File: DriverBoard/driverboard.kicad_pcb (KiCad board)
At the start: 2 copper layers, 95 x 95 mm, 93 parts, among them J1 USB_C_Receptacle_USB2.0_14P, J2 Conn_01x02_Pin, J3 Conn_02x05_Counter_Clockwise, J4 Conn_02x05_Counter_Clockwise, J5 Conn_02x05_Counter_Clockwise, J6 Conn_01x08_Pin, J7 Conn_01x08_Pin, J8 Conn_01x08_Pin, J9 Conn_01x08_Pin, Q1 DMG2305UX, Q2 DMG2305UX, Q3 SL3402, Q4 SL3402, Q5 SL3402, Q6 SL3402, U1 LM556, U10 74HC595, U11 TBD62783A, U2 MC34063AD, U3 TLV274, U4 74HC595, U5 TBD62783A, U6 74HC595, U7 TBD62783A, U8 74HC595, U9 TBD62783A

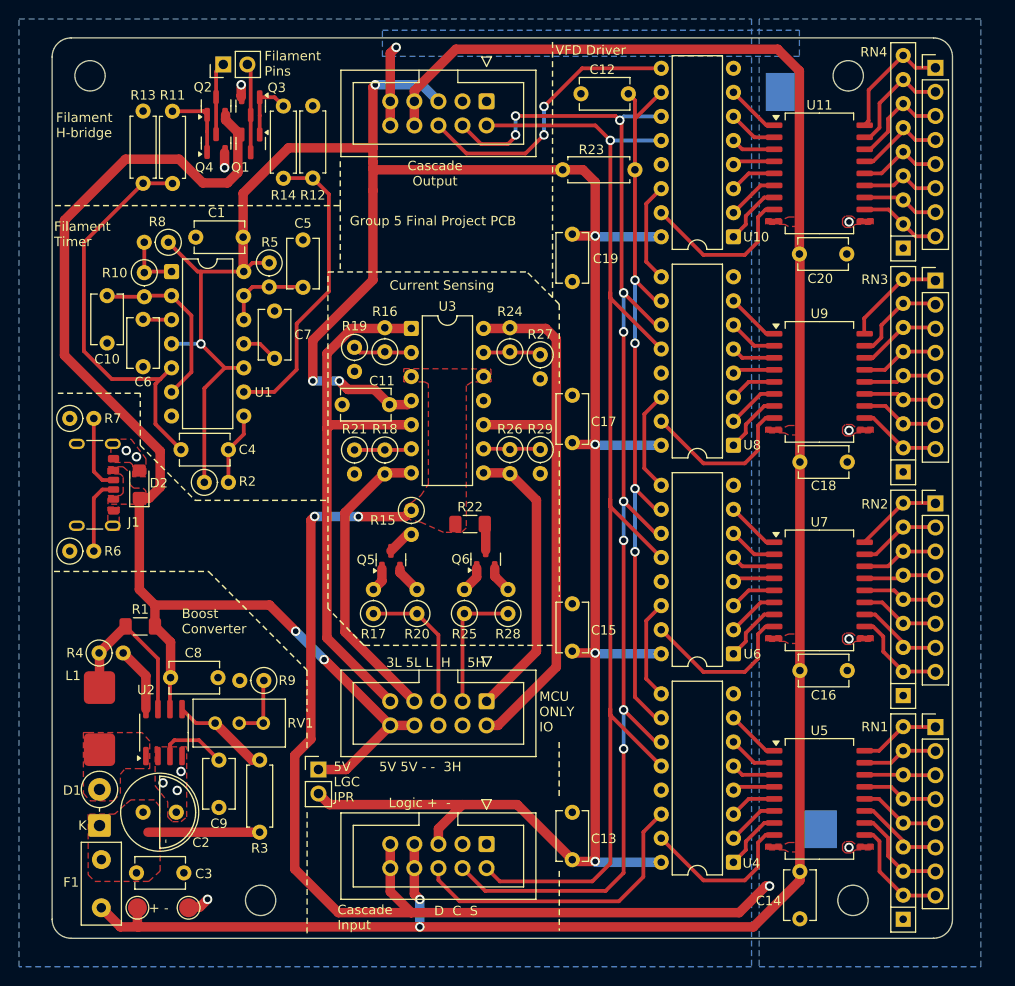
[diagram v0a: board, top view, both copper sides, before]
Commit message: Minor PCB rev
Moved shift register bypass caps around a bit. Also changed a price on
the BOM, that's the final change before the digikey parts order is in.
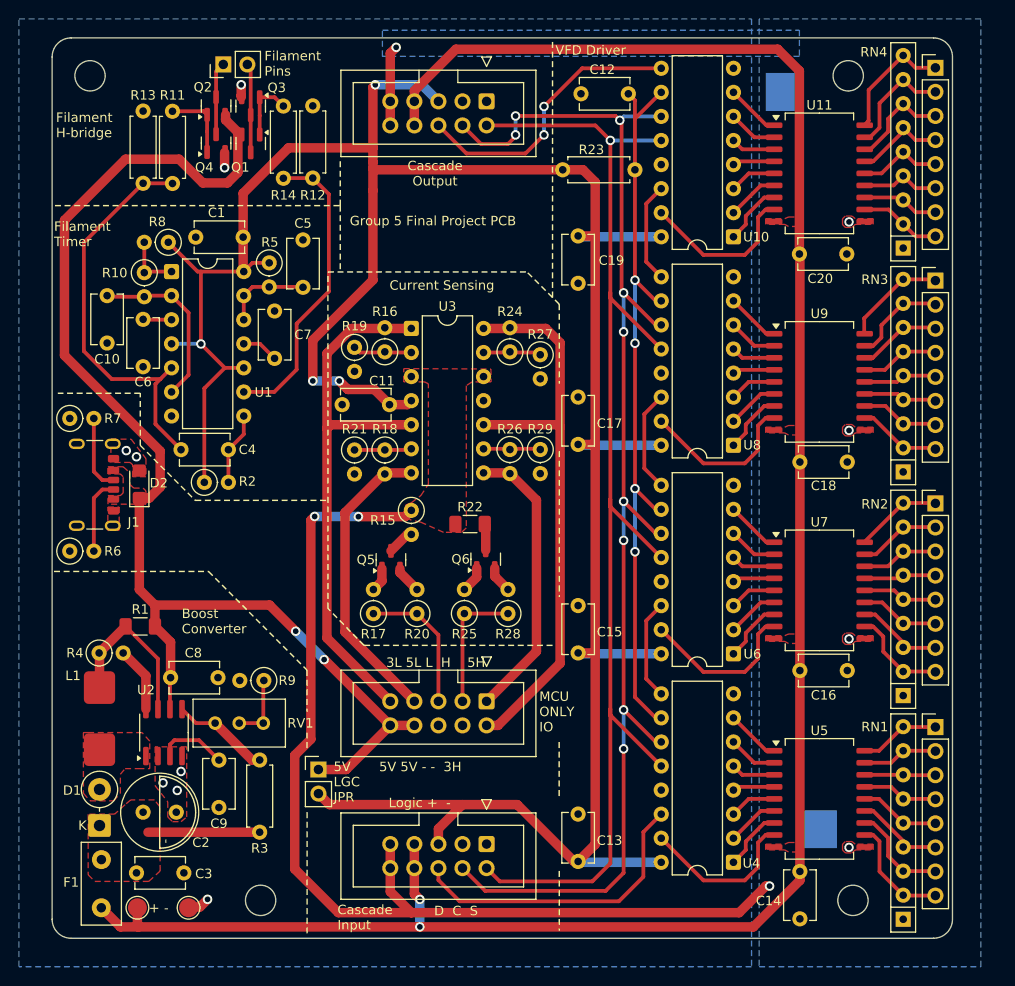
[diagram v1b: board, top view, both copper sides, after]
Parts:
- moved C13 0.64 mm to (168.9, 130.2)
- moved C15 0.64 mm to (168.9, 108.2)
- moved C17 0.64 mm to (168.9, 86.2)
- moved C19 0.64 mm to (168.9, 64.2)
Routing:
- net VCC: track 286.0 -> 291.1 mm, vias 8 -> 4
- net 3HCS: track 60.4 -> 61.2 mm

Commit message: Fixed H-bridge timer
The H-bridge timer had no blank time on a clock transition before, this
would cause a momentary short circuit as the mosfet switching times
aren't instant. To fix this an extra 555 timer stage was added.
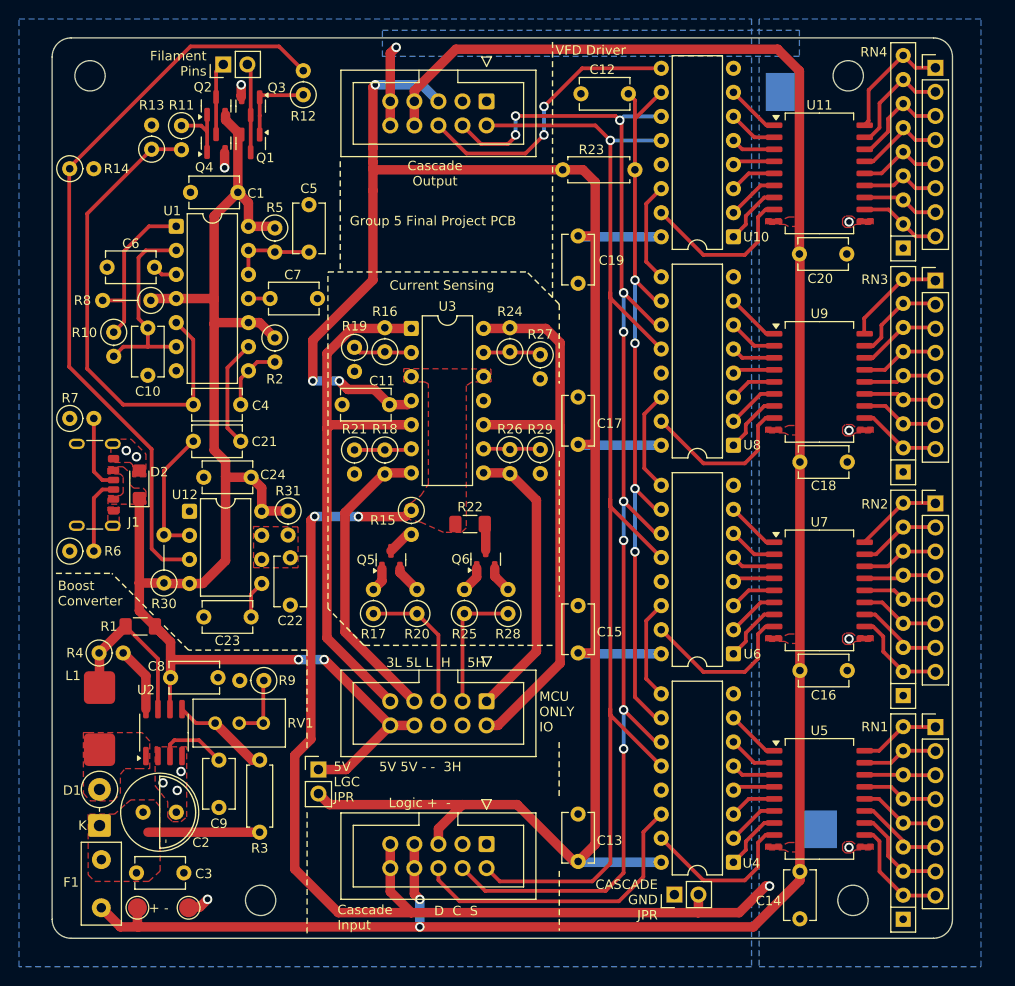
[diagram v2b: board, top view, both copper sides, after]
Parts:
- added C21: 10n, Capacitor_THT:C_Disc_D5.1mm_W3.2mm_P5.00mm, F.Cu at (133.3, 85.9)
- added C22: 220n, Capacitor_THT:C_Disc_D5.1mm_W3.2mm_P5.00mm, F.Cu at (138.5, 98.2)
- added C23: 10n, Capacitor_THT:C_Disc_D5.1mm_W3.2mm_P5.00mm, F.Cu at (134.4, 104.4)
- added C24: 100n, Capacitor_THT:C_Disc_D5.1mm_W3.2mm_P5.00mm, F.Cu at (134.4, 89.7)
- added JP2: Jumper_2_Open, Connector_PinHeader_2.54mm:PinHeader_1x02_P2.54mm_Vertical, F.Cu at (179.1, 133.7)
- added R30: 3k3, Resistor_THT:R_Axial_DIN0207_L6.3mm_D2.5mm_P5.08mm_Vertical, F.Cu at (125.2, 100.8)
- added R31: 39k, Resistor_THT:R_Axial_DIN0207_L6.3mm_D2.5mm_P2.54mm_Vertical, F.Cu at (138.3, 93.2)
- added U12: LM555xN, Package_DIP:DIP-8_W7.62mm, F.Cu at (127.9, 93.3)
- C4: value 1n -> 10n
- C5: value 220n -> 10n
- R11, R12, R13, R14: footprint Resistor_THT:R_Axial_DIN0207_L6.3mm_D2.5mm_P7.62mm_Horizontal -> Resistor_THT:R_Axial_DIN0207_L6.3mm_D2.5mm_P2.54mm_Vertical
- R2: value 33k -> 3k3
- R5: value 39k -> 10k
- R8: footprint Resistor_THT:R_Axial_DIN0207_L6.3mm_D2.5mm_P2.54mm_Vertical -> Resistor_THT:R_Axial_DIN0207_L6.3mm_D2.5mm_P5.08mm_Vertical
- moved R14 25.7 mm to (115.3, 57.1), turned to 0 degrees
- moved R2 17.0 mm to (136.9, 75.0), turned to -90 degrees
- moved R10 7.06 mm to (119.9, 74.4)
- moved R8 6.41 mm to (123.8, 71.0)
- moved C7 6.33 mm to (136.4, 70.8), turned to 0 degrees
- moved C6 5.62 mm to (124.2, 67.5), turned to 180 degrees
- moved C10 5.48 mm to (123.5, 73.9)
- moved C4 4.92 mm to (128.3, 82.0)
- moved U1 4.80 mm to (126.5, 63.2)
- moved C1 4.76 mm to (133.0, 59.6)
- moved C5 3.77 mm to (140.5, 65.9)
- moved R5 3.73 mm to (136.9, 63.4)
- moved R13 3.71 mm to (123.9, 55.0)
- moved R12 2.41 mm to (139.9, 49.3), turned to 90 degrees
- moved R11 1.79 mm to (127.0, 52.6)
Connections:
- C1 pad 1: VCC -> +5V
- R2 pad 1: VCC -> +5V
- R5 pad 1: VCC -> +5V
- R8 pad 1: VCC -> +5V
- U1 pad 10: VCC -> +5V
- U1 pad 14: VCC -> +5V
- U1 pad 4: VCC -> +5V
- U1 pad 9: H2 -> /TIM_2_OUT
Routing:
- net VCC: track 291.1 -> 225.6 mm, vias 4 -> 3
- net H2: track 32.0 -> 79.3 mm
- net +5V: track 129.8 -> 152.7 mm
- net /TIM_3_IN: track 0.00 -> 13.9 mm
- net /TIM_1_DIS: track 5.96 -> 17.9 mm
- net /TIM_2_OUT: track 0.00 -> 11.5 mm
- net H1: track 43.1 -> 51.3 mm
- net /TIM_3_CV: track 0.00 -> 3.99 mm
- net /TIMING_CAP_1: track 18.2 -> 21.1 mm
- net GNDA: track 118.4 -> 120.3 mm
- net BRIDGE_G2: track 6.82 -> 8.65 mm
- net /TIM_2_CV: track 3.89 -> 2.28 mm
- net BRIDGE_G1: track 7.73 -> 6.88 mm
- net /TIM_2_IN: track 7.67 -> 7.09 mm
- added copper zone on F.Cu, net /TIMING_CAP_3
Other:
- board text added: "CASCADE GND JPR"
- board text removed: "Filament H-bridge"
- board text removed: "Filament Timer"

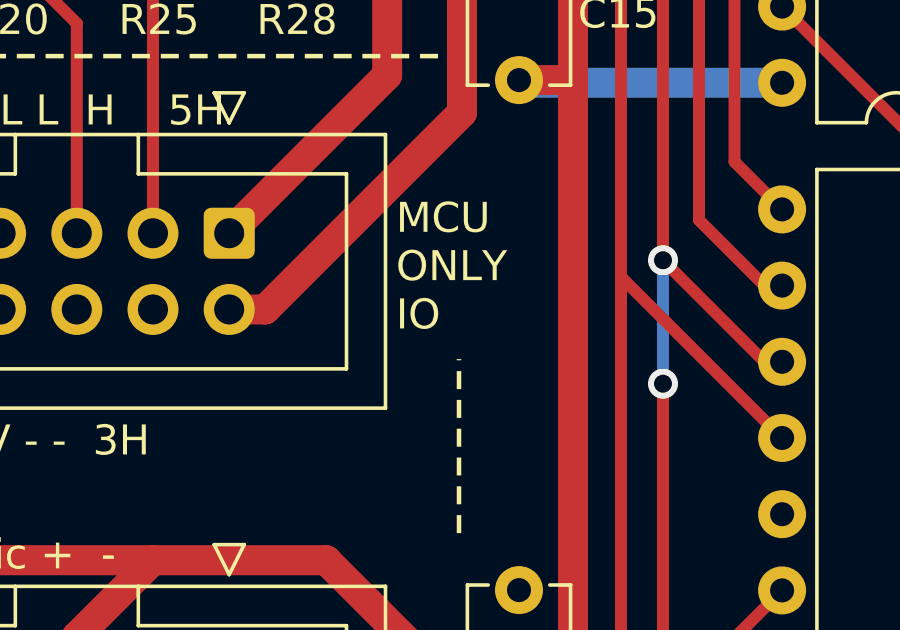
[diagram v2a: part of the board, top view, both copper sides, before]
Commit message: Updated shield
Also made driver board a bit tider
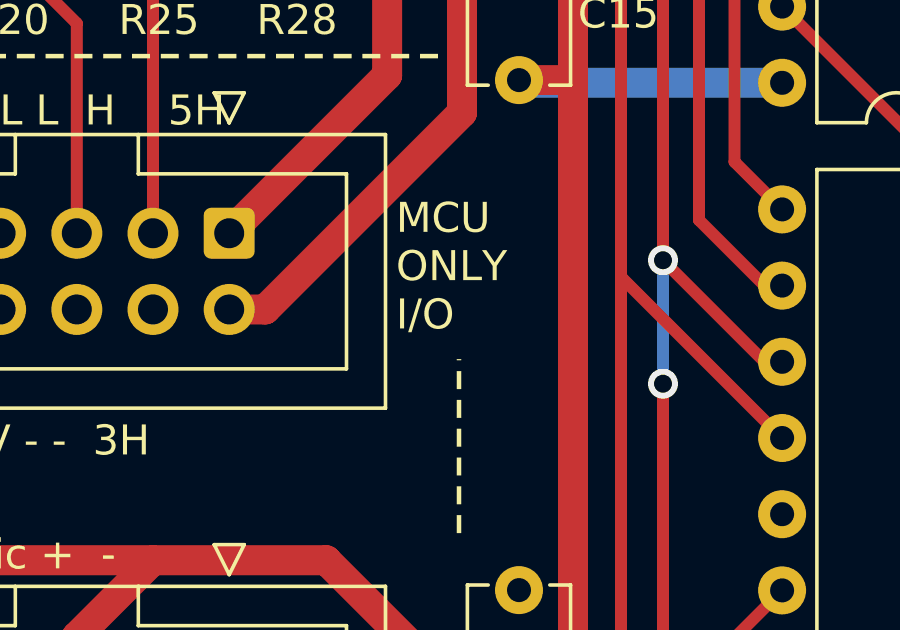
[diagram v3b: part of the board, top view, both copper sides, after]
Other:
- board text added: "MCU ONLY I/O"
- board text removed: "MCU ONLY IO"
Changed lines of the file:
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@@
 	(title_block
 		(title "Generic VFD Driver PCB")
-		(date "2025-10-04")
+		(date "2025-10-05")
 		(rev "9")
 		(company "ENEL200")
@@
 			)
 		)
+		(property "Digikey Part No" "UC"
+			(at 0 0 0)
+			(unlocked yes)
+			(layer "F.Fab")
+			(hide yes)
+			(effects
+				(font
+					(size 1 1)
+					(thickness 0.15)
+				)
+			)
+		)
+		(property "Manufacturer Part No" "LM555"
+			(at 0 0 0)
+			(unlocked yes)
+			(layer "F.Fab")
+			(hide yes)
+			(effects
+				(font
+					(size 1 1)
+					(thickness 0.15)
+				)
+			)
+		)
+		(property "Master Component" "1"
+			(at 0 0 0)
+			(unlocked yes)
+			(layer "F.Fab")
+			(hide yes)
+			(effects
+				(font
+					(size 1 1)
+					(thickness 0.15)
+				)
+			)
+		)
+		(property "Unit Price ($)" "3"
+			(at 0 0 0)
+			(unlocked yes)
+			(layer "F.Fab")
+			(hide yes)
+			(effects
+				(font
+					(size 1 1)
+					(thickness 0.15)
+				)
+			)
+		)
 		(property ki_fp_filters "DIP*W7.62mm*")
 		(sheetname "/")
@@
 			)
 		)
-		(property "Unit Price ($)" "0.40"
+		(property "Unit Price ($)" "0.20"
 			(at 0 0 90)
 			(unlocked yes)
@@
 		)
 	)
-	(gr_text "MCU\nONLY\nIO"
+	(gr_text "MCU\nONLY\nI/O"
 		(at 164.8 116.6 0)
 		(layer "F.SilkS")

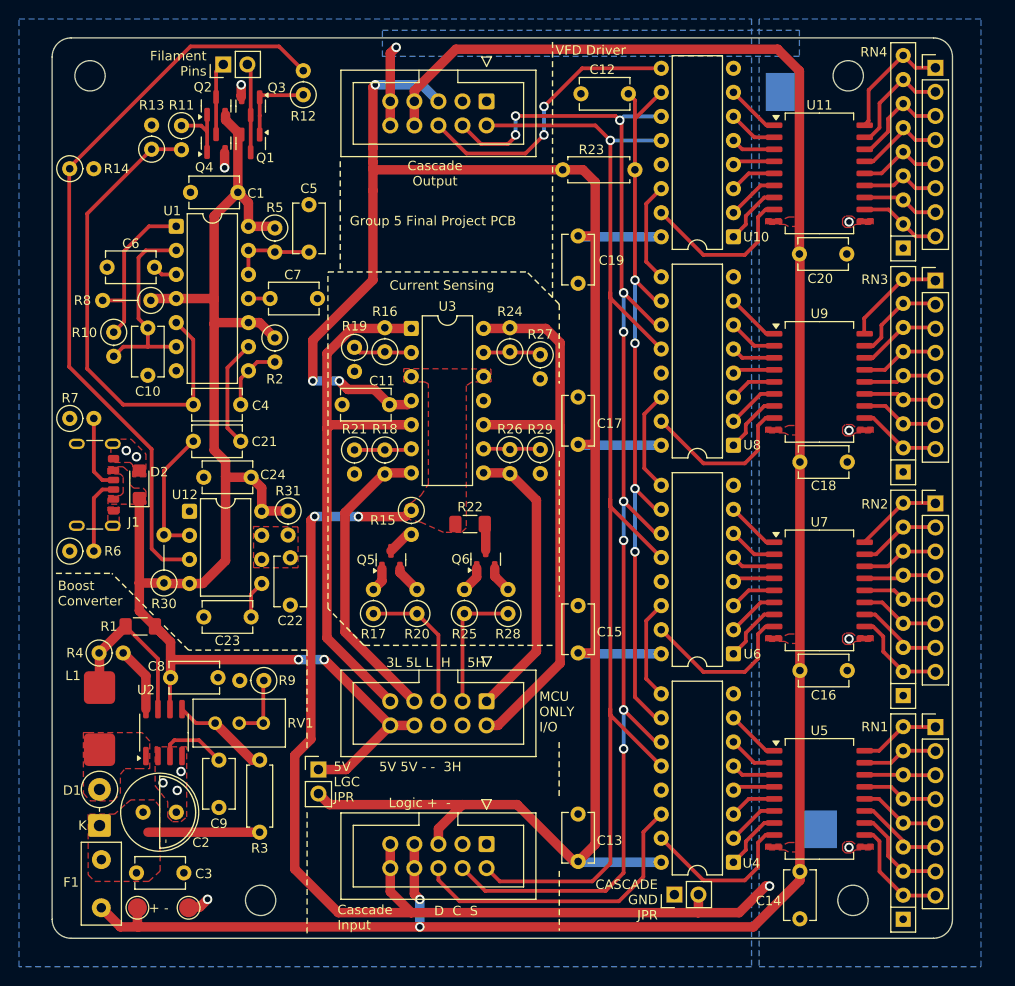
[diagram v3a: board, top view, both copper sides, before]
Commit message: Removed Current Sensing
Removed current sensing, because it would require a major design
overhaul to work properly.
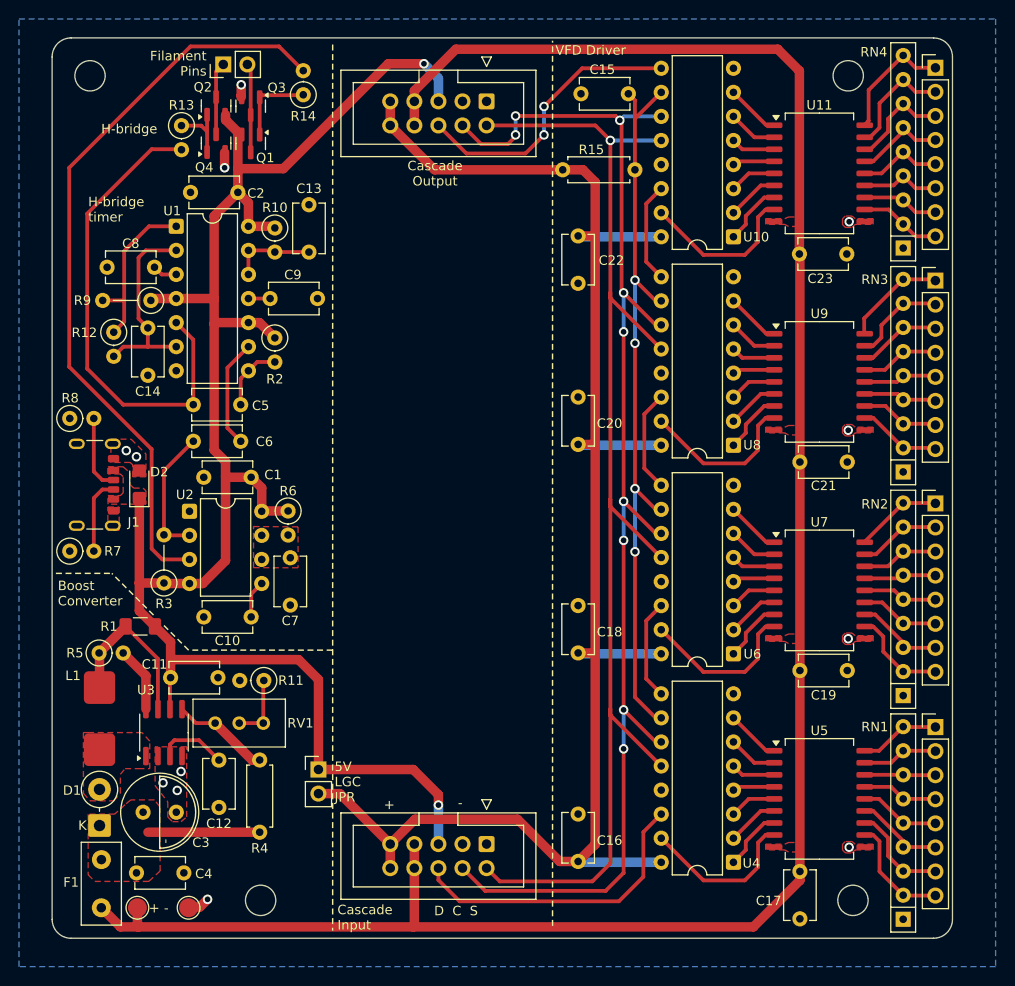
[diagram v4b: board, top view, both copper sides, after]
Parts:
- removed the C11 at (149.0, 82.0)
- removed the J4 at (159.2, 113.3)
- removed JP2: Jumper_2_Open, Connector_PinHeader_2.54mm:PinHeader_1x02_P2.54mm_Vertical
- removed Q5, Q6: SL3402, Package_TO_SOT_SMD:SOT-23
- removed the R13 at (123.9, 55.0)
- removed the R14 at (115.3, 57.1)
- removed the R15 at (151.3, 93.2)
- removed R16: 12k, Resistor_THT:R_Axial_DIN0207_L6.3mm_D2.5mm_P2.54mm_Vertical
- removed R17, R25: 2K2, Resistor_THT:R_Axial_DIN0207_L6.3mm_D2.5mm_P2.54mm_Vertical
- removed R18, R20, R21, R26, R28, R29: 10k, Resistor_THT:R_Axial_DIN0207_L6.3mm_D2.5mm_P2.54mm_Vertical
- removed R19, R27: 100R, Resistor_THT:R_Axial_DIN0207_L6.3mm_D2.5mm_P2.54mm_Vertical
- removed R22: 0.2R, Resistor_SMD:R_1206_3216Metric_Pad1.30x1.75mm_HandSolder
- removed R24: 18k, Resistor_THT:R_Axial_DIN0207_L6.3mm_D2.5mm_P2.54mm_Vertical
- removed the TP1 at (190.7, 49.0)
- removed the TP2 at (194.2, 126.8)
- removed the U3 at (151.3, 74.0)
- renumbered C24 to C1, C23 to C10, C8 to C11, C9 to C12, C5 to C13, C10 to C14, C12 to C15, C13 to C16, C14 to C17, C15 to C18, C16 to C19, C1 to C2, C17 to C20, C18 to C21, C19 to C22, C20 to C23, C2 to C3, C3 to C4, C4 to C5, C21 to C6, C22 to C7, C6 to C8, C7 to C9, J5 to J4, J6 to J5, J7 to J6, J8 to J7, J9 to J8, R5 to R10, R9 to R11, R10 to R12, R11 to R13, R12 to R14, R23 to R15, R30 to R3, R3 to R4, R4 to R5, R31 to R6, R6 to R7, R7 to R8, R8 to R9, TP3 to TP1, TP4 to TP2, U12 to U2, U2 to U3
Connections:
- C17 pad 2: GNDA -> GND
- C19 pad 2: GNDA -> GND
- C21 pad 2: GNDA -> GND
- C23 pad 2: GNDA -> GND
- J3 pad 10: GNDA -> VCC
- J3 pad 5: VCC -> +5V
- J3 pad 9: GNDA -> VCC
- J4 pad 10: GNDA -> VCC
- J4 pad 5: VCC -> +5V
- J4 pad 9: GNDA -> VCC
- RN1 pad 1: GNDA -> GND
- RN2 pad 1: GNDA -> GND
- RN3 pad 1: GNDA -> GND
- RN4 pad 1: GNDA -> GND
- U11 pad 10: GNDA -> GND
- U5 pad 10: GNDA -> GND
- U7 pad 10: GNDA -> GND
- U9 pad 10: GNDA -> GND
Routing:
- net GNDA: track 120.3 -> 0.00 mm, vias 8 -> 0
- net 3HCS: track 61.2 -> 0.00 mm
- net 3LCS: track 58.5 -> 0.00 mm
- net VCC: track 225.6 -> 174.3 mm, vias 3 -> 0
- net +5V: track 152.7 -> 186.3 mm
- net 5LCS: track 31.4 -> 0.00 mm
- net 5HCS: track 30.1 -> 0.00 mm
- net LCS_EN: track 14.8 -> 0.00 mm
- net HCS_EN: track 13.7 -> 0.00 mm
- net /AFB: track 6.22 -> 0.00 mm
- net /CFB: track 5.91 -> 0.00 mm
- net /BFB: track 5.88 -> 0.00 mm
- net GND: track 10.9 -> 5.16 mm, vias 8 -> 12
- net /DFB: track 5.75 -> 0.00 mm
- net /LCS_DRAIN: track 2.87 -> 0.00 mm
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- removed copper zone on B.Cu, net GNDA
- removed copper zone on F.Cu, net GNDA
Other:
- board text added: "H-bridge"
- board text added: "H-bridge timer"
- board text removed: "3L 5L L H 5H"
- board text removed: "5V 5V - - 3H"
- board text removed: "CASCADE GND JPR"
- board text removed: "Current Sensing"
- board text removed: "Group 5 Final Project PCB"
- board text removed: "Logic + -"
- board text removed: "MCU ONLY I/O"
- board text removed: "The current sensing lines to MCU are thick to minimise voltage drop (voltage drop would minimise dynamic range)"
